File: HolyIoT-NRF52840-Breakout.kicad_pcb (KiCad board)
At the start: 2 copper layers, 45 x 35 mm, 7 parts, among them J1 Conn_01x13_Male, J2 Conn_01x09_Male, J3 Conn_01x11_Male, J4 Conn_01x13_Male, J5 Conn_01x09_Male, U1 HolyIOT_NRF52840

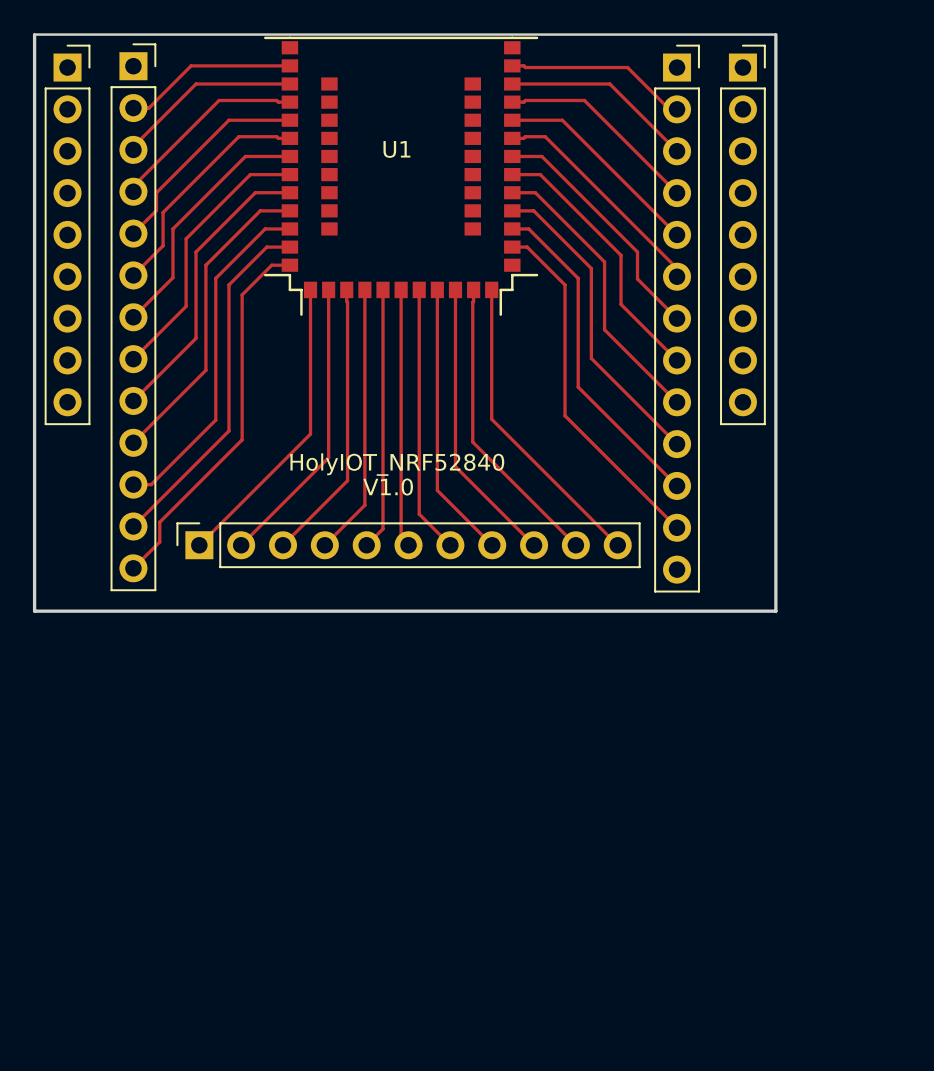
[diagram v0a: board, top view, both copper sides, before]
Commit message: Routing done
Last thing to do : labelling
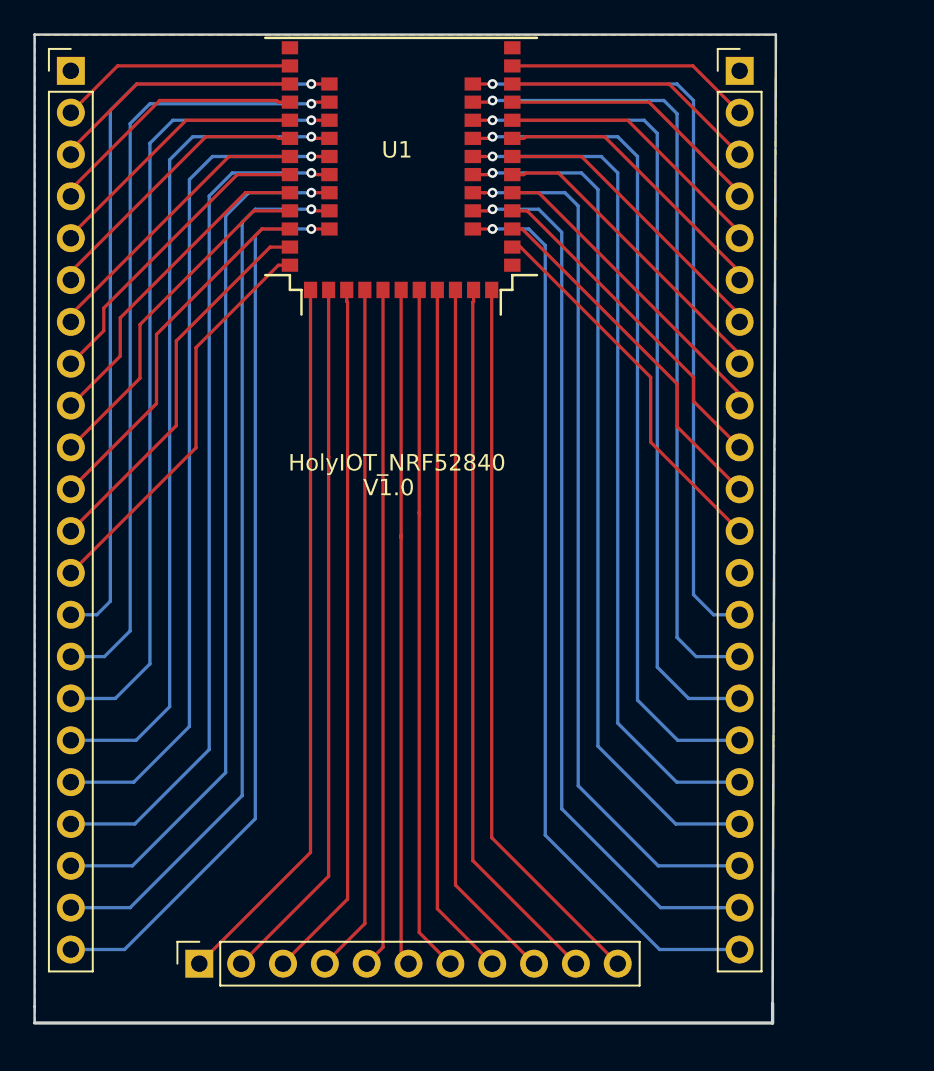
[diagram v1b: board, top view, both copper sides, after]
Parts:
- removed G***: LOGO, MWL:Serigraphie
- removed J4: Conn_01x13_Male, Connector_PinSocket_2.54mm:PinSocket_1x13_P2.54mm_Vertical
- removed J5: Conn_01x09_Male, Connector_PinSocket_2.54mm:PinSocket_1x09_P2.54mm_Vertical
- J1: value Conn_01x13_Male -> Conn_01x22_Male; footprint Connector_PinSocket_2.54mm:PinSocket_1x13_P2.54mm_Vertical -> Connector_PinHeader_2.54mm:PinHeader_1x22_P2.54mm_Vertical
- J2: value Conn_01x09_Male -> Conn_01x22_Male; footprint Connector_PinSocket_2.54mm:PinSocket_1x09_P2.54mm_Vertical -> Connector_PinHeader_2.54mm:PinHeader_1x22_P2.54mm_Vertical
- moved J2 40.8 mm to (138.8, 84.2)
- moved J3 25.4 mm to (106.0, 138.4)
- moved J1 3.81 mm to (98.2, 84.2)
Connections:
- J2 pad 1: Net-(J2-Pad1) -> GND
- U1 pad 14: Net-(J2-Pad1) -> Net-(J1-Pad14)
- U1 pad 15: Net-(J2-Pad2) -> Net-(J1-Pad15)
- U1 pad 16: Net-(J2-Pad3) -> Net-(J1-Pad16)
- U1 pad 17: Net-(J2-Pad4) -> Net-(J1-Pad17)
- U1 pad 18: Net-(J2-Pad5) -> Net-(J1-Pad18)
- U1 pad 19: Net-(J2-Pad6) -> Net-(J1-Pad19)
- U1 pad 20: Net-(J2-Pad7) -> Net-(J1-Pad20)
- U1 pad 21: Net-(J2-Pad8) -> Net-(J1-Pad21)
- U1 pad 22: Net-(J2-Pad9) -> Net-(J1-Pad22)
- U1 pad 23: Net-(J5-Pad1) -> Net-(J2-Pad14)
- U1 pad 24: Net-(J5-Pad2) -> Net-(J2-Pad15)
- U1 pad 25: Net-(J5-Pad3) -> Net-(J2-Pad16)
- U1 pad 26: Net-(J5-Pad4) -> Net-(J2-Pad17)
- U1 pad 27: Net-(J5-Pad5) -> Net-(J2-Pad18)
- U1 pad 28: Net-(J5-Pad6) -> Net-(J2-Pad19)
- U1 pad 29: Net-(J5-Pad7) -> Net-(J2-Pad20)
- U1 pad 30: Net-(J5-Pad8) -> Net-(J2-Pad21)
- U1 pad 31: Net-(J5-Pad9) -> Net-(J2-Pad22)
- U1 pad 33: Net-(J4-Pad2) -> Net-(J2-Pad2)
- U1 pad 34: Net-(J4-Pad3) -> Net-(J2-Pad3)
- U1 pad 35: Net-(J4-Pad4) -> Net-(J2-Pad4)
- U1 pad 36: Net-(J4-Pad5) -> Net-(J2-Pad5)
- U1 pad 37: Net-(J4-Pad6) -> Net-(J2-Pad6)
- U1 pad 38: Net-(J4-Pad7) -> Net-(J2-Pad7)
- U1 pad 39: Net-(J4-Pad8) -> Net-(J2-Pad8)
- U1 pad 40: Net-(J4-Pad9) -> Net-(J2-Pad9)
- U1 pad 41: Net-(J4-Pad10) -> Net-(J2-Pad10)
- U1 pad 42: Net-(J4-Pad11) -> Net-(J2-Pad11)
- U1 pad 43: Net-(J4-Pad12) -> Net-(J2-Pad12)
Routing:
- net Net-(J2-Pad22): track 0.00 -> 55.3 mm, vias 0 -> 1
- net Net-(J1-Pad22): track 0.00 -> 54.6 mm, vias 0 -> 1
- net Net-(J2-Pad21): track 0.00 -> 54.3 mm, vias 0 -> 1
- net Net-(J2-Pad20): track 0.00 -> 53.7 mm, vias 0 -> 1
- net Net-(J1-Pad21): track 0.00 -> 53.7 mm, vias 0 -> 1
- net Net-(J1-Pad20): track 0.00 -> 52.4 mm, vias 0 -> 1
- net Net-(J2-Pad19): track 0.00 -> 52.4 mm, vias 0 -> 1
- net Net-(J1-Pad19): track 0.00 -> 51.8 mm, vias 0 -> 1
- net Net-(J2-Pad18): track 0.00 -> 51.5 mm, vias 0 -> 1
- net Net-(J1-Pad18): track 0.00 -> 50.9 mm, vias 0 -> 1
- net Net-(J2-Pad17): track 0.00 -> 50.7 mm, vias 0 -> 1
- net Net-(J1-Pad17): track 0.00 -> 50.4 mm, vias 0 -> 1
- net Net-(J2-Pad16): track 0.00 -> 49.7 mm, vias 0 -> 1
- net Net-(J2-Pad15): track 0.00 -> 48.9 mm, vias 0 -> 1
- net Net-(J1-Pad16): track 0.00 -> 48.7 mm, vias 0 -> 1
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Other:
- board size 45 x 35 mm -> 45 x 60 mm
- net class Default: clearance 0.2 -> 0.3
- rule trace_clearance: 0.2 -> 0.3

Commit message: Add some serigraphie
Add some serigraphie
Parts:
- U1: value HolyIOT_NRF52840 -> HolyIOT_NRF52840_Module
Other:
- board text added: "GND"
- board text added: "P0.02"
- board text added: "P0.03"
- board text added: "P0.04"
- board text added: "P0.05"
- board text added: "P0.06"
- board text added: "P0.08"
- board text added: "P0.11"
- board text added: "P0.25"
- board text added: "P0.26"
- board text added: "P0.27"
- board text added: "P0.28"
- board text added: "P0.29"
- board text added: "P0.30"
- board text added: "P0.31"
- board text added: "P1.08"
- board text added: "P1.10"
- board text added: "P1.11"
- board text added: "P1.12"
- board text added: "P1.13"
- board text added: "P1.14"
- board text added: "P1.15"
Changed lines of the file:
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@@
   (general
     (thickness 1.6)
-    (drawings 9)
+    (drawings 31)
     (tracks 254)
     (zones 0)
@@
     (uvia_min_size 0.2)
     (uvia_min_drill 0.1)
-    (pcb_text_width 0.3)
-    (pcb_text_size 1.5 1.5)
+    (pcb_text_width 0.15)
+    (pcb_text_size 1 1)
     (mod_edge_width 0.15)
     (mod_text_size 1 1)
@@
       (effects (font (size 1 1) (thickness 0.15)))
     )
-    (fp_text value HolyIOT_NRF52840 (at 0 12) (layer F.SilkS)
+    (fp_text value HolyIOT_NRF52840_Module (at 0 12) (layer F.SilkS)
       (effects (font (size 1 1) (thickness 0.15)))
     )
@@
     )
   )
+  (gr_text P0.26 (at 102.2 137.4) (layer F.SilkS)
+    (effects (font (size 1 1) (thickness 0.15)))
+  )
+  (gr_text P0.06 (at 102.2 134.8) (layer F.SilkS)
+    (effects (font (size 1 1) (thickness 0.15)))
+  )
+  (gr_text P0.08 (at 102.2 132.4) (layer F.SilkS)
+    (effects (font (size 1 1) (thickness 0.15)))
+  )
+  (gr_text P0.27 (at 102.2 129.8) (layer F.SilkS)
+    (effects (font (size 1 1) (thickness 0.15)))
+  )
+  (gr_text P1.08 (at 102.2 127.2) (layer F.SilkS)
+    (effects (font (size 1 1) (thickness 0.15)))
+  )
+  (gr_text P0.11 (at 102.2 124.8) (layer F.SilkS)
+    (effects (font (size 1 1) (thickness 0.15)))
+  )
+  (gr_text P0.25 (at 102.2 122.2) (layer F.SilkS)
+    (effects (font (size 1 1) (thickness 0.15)))
+  )
+  (gr_text P1.12 (at 102.2 119.6) (layer F.SilkS)
+    (effects (font (size 1 1) (thickness 0.15)))
+  )
+  (gr_text P1.14 (at 102.2 117.2) (layer F.SilkS)
+    (effects (font (size 1 1) (thickness 0.15)))
+  )
+  (gr_text P0.05 (at 102.2 114.6) (layer F.SilkS)
+    (effects (font (size 1 1) (thickness 0.15)))
+  )
+  (gr_text "P0.04\n\n" (at 102.2 113) (layer F.SilkS)
+    (effects (font (size 1 1) (thickness 0.15)))
+  )
+  (gr_text "P0.31\n\n" (at 102.2 110.4) (layer F.SilkS)
+    (effects (font (size 1 1) (thickness 0.15)))
+  )
+  (gr_text "P0.30\n\n" (at 102.2 107.8) (layer F.SilkS)
+    (effects (font (size 1 1) (thickness 0.15)))
+  )
+  (gr_text "P0.29\n" (at 102.2 104.4) (layer F.SilkS)
+    (effects (font (size 1 1) (thickness 0.15)))
+  )
+  (gr_text "P0.28\n\n" (at 102.2 102.8) (layer F.SilkS)
+    (effects (font (size 1 1) (thickness 0.15)))
+  )
+  (gr_text "P0.02\n\n" (at 102.2 100.2) (layer F.SilkS)
+    (effects (font (size 1 1) (thickness 0.15)))
+  )
+  (gr_text "P0.03\n\n" (at 102.2 97.6) (layer F.SilkS)
+    (effects (font (size 1 1) (thickness 0.15)))
+  )
+  (gr_text "P1.15\n\n" (at 102.2 95.2) (layer F.SilkS)
+    (effects (font (size 1 1) (thickness 0.15)))
+  )
+  (gr_text "P1.13\n\n" (at 102.2 92.6) (layer F.SilkS)
+    (effects (font (size 1 1) (thickness 0.15)))
+  )
+  (gr_text "P1.11\n\n" (at 102.2 90) (layer F.SilkS)
+    (effects (font (size 1 1) (thickness 0.15)))
+  )
+  (gr_text "P1.10\n" (at 102.2 86.6) (layer F.SilkS)
+    (effects (font (size 1 1) (thickness 0.15)))
+  )
+  (gr_text GND (at 101.6 84) (layer F.SilkS)
+    (effects (font (size 1 1) (thickness 0.15)))
+  )
   (gr_line (start 96 141) (end 96 142) (layer Edge.Cuts) (width 0.15))

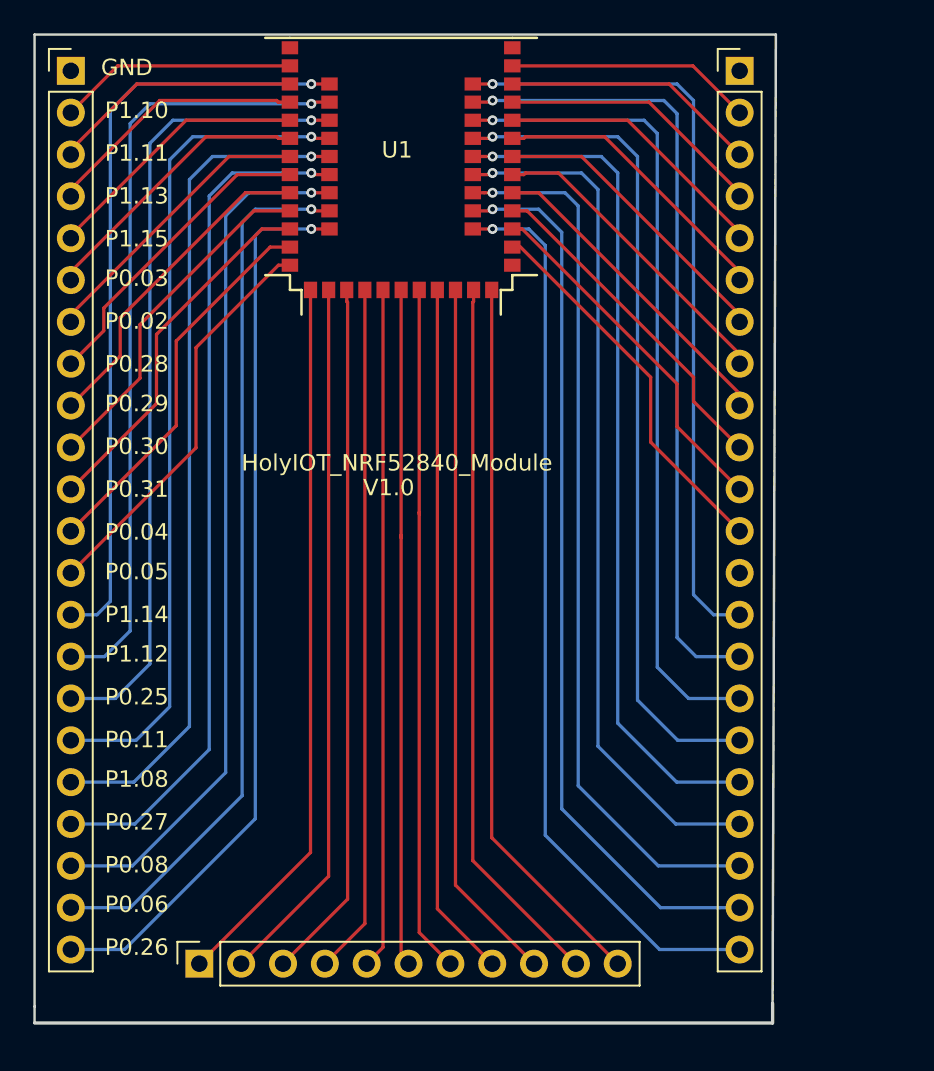
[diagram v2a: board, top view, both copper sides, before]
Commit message: Finish PCB V1.0
Add missing serigraphie
test via under pad
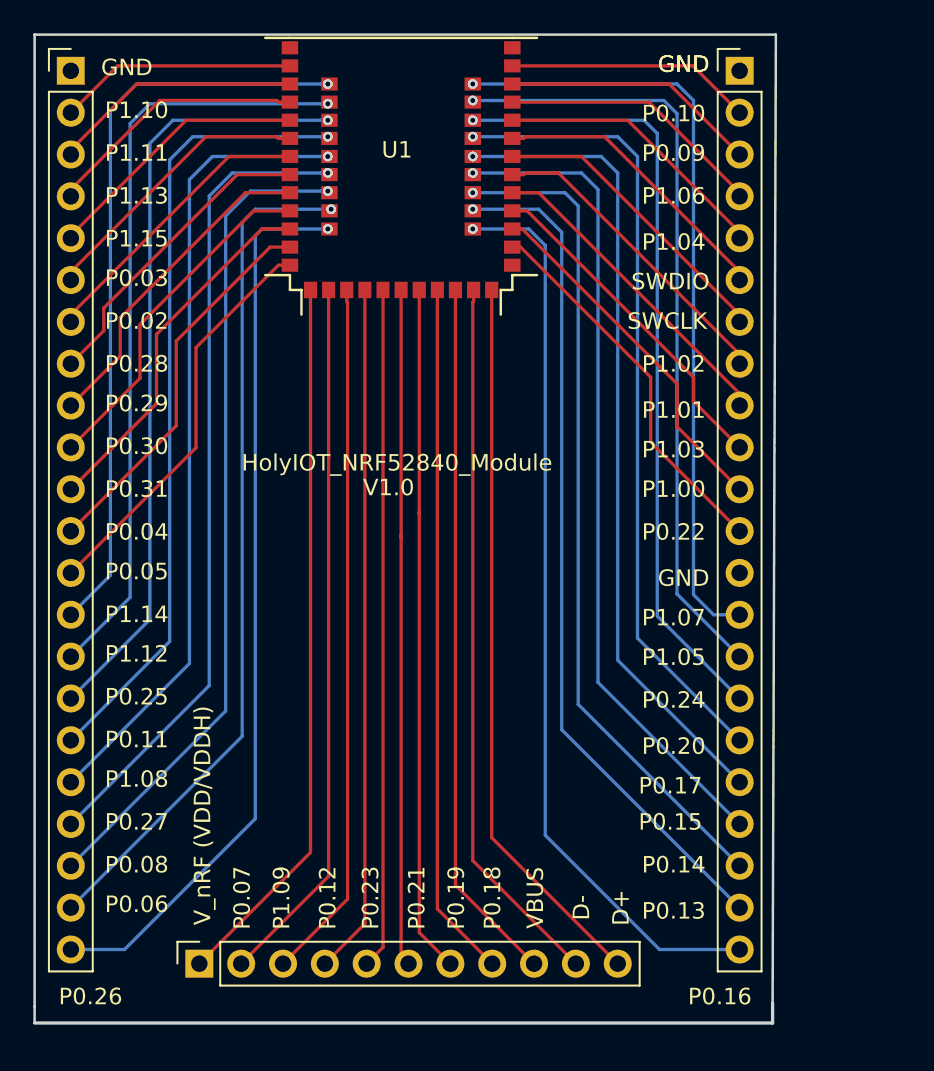
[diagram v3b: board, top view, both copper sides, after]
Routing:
- net Net-(J2-Pad20): track 53.7 -> 50.9 mm
- net Net-(J2-Pad21): track 54.3 -> 51.5 mm
- net Net-(J1-Pad17): track 50.4 -> 47.9 mm
- net Net-(J1-Pad19): track 51.8 -> 49.4 mm
- net Net-(J1-Pad18): track 50.9 -> 48.5 mm
- net Net-(J2-Pad19): track 52.4 -> 50.1 mm
- net Net-(J1-Pad20): track 52.4 -> 50.2 mm
- net Net-(J2-Pad17): track 50.7 -> 48.5 mm
- net Net-(J2-Pad18): track 51.5 -> 49.3 mm
- net Net-(J1-Pad21): track 53.7 -> 51.6 mm
- net Net-(J2-Pad16): track 49.7 -> 47.9 mm
- net Net-(J1-Pad16): track 48.7 -> 47.1 mm
- net Net-(J2-Pad15): track 48.9 -> 47.3 mm
- net Net-(J1-Pad15): track 47.7 -> 46.3 mm
- net Net-(J1-Pad14): track 46.5 -> 45.5 mm
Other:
- board text added: "D+"
- board text added: "D-"
- board text added: "P0.07"
- board text added: "P0.09"
- board text added: "P0.10"
- board text added: "P0.12"
- board text added: "P0.13"
- board text added: "P0.14"
- board text added: "P0.15"
- board text added: "P0.16"
- board text added: "P0.17"
- board text added: "P0.18"
- board text added: "P0.19"
- board text added: "P0.20"
- board text added: "P0.21"
- board text added: "P0.22"
- board text added: "P0.23"
- board text added: "P0.24"
- board text added: "P1.00"
- board text added: "P1.01"
- board text added: "P1.02"
- board text added: "P1.03"
- board text added: "P1.04"
- board text added: "P1.05"
- board text added: "P1.06"
- board text added: "P1.07"
- board text added: "P1.09"
- board text added: "SWCLK"
- board text added: "SWDIO"
- board text added: "VBUS"
- board text added: "V_nRF (VDD/VDDH)"

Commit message: Fornet the netlist
^^
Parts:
- U1: value HolyIOT_NRF52840_Module -> HolyIOT_NRF52840
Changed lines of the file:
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@@
       (effects (font (size 1 1) (thickness 0.15)))
     )
-    (fp_text value HolyIOT_NRF52840_Module (at 0 12) (layer F.SilkS)
+    (fp_text value HolyIOT_NRF52840 (at 0 12) (layer F.SilkS)
       (effects (font (size 1 1) (thickness 0.15)))
     )

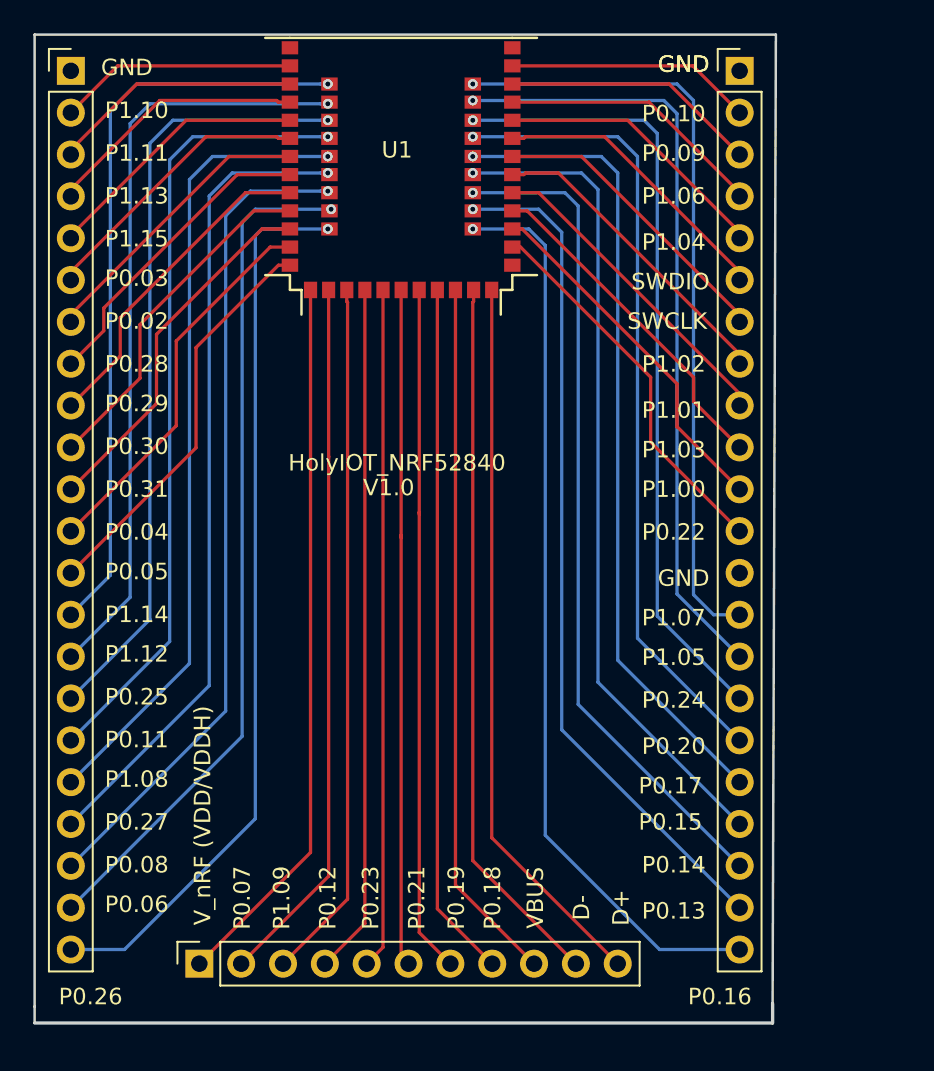
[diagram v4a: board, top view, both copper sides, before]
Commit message: micro-usb b
add micro-usb
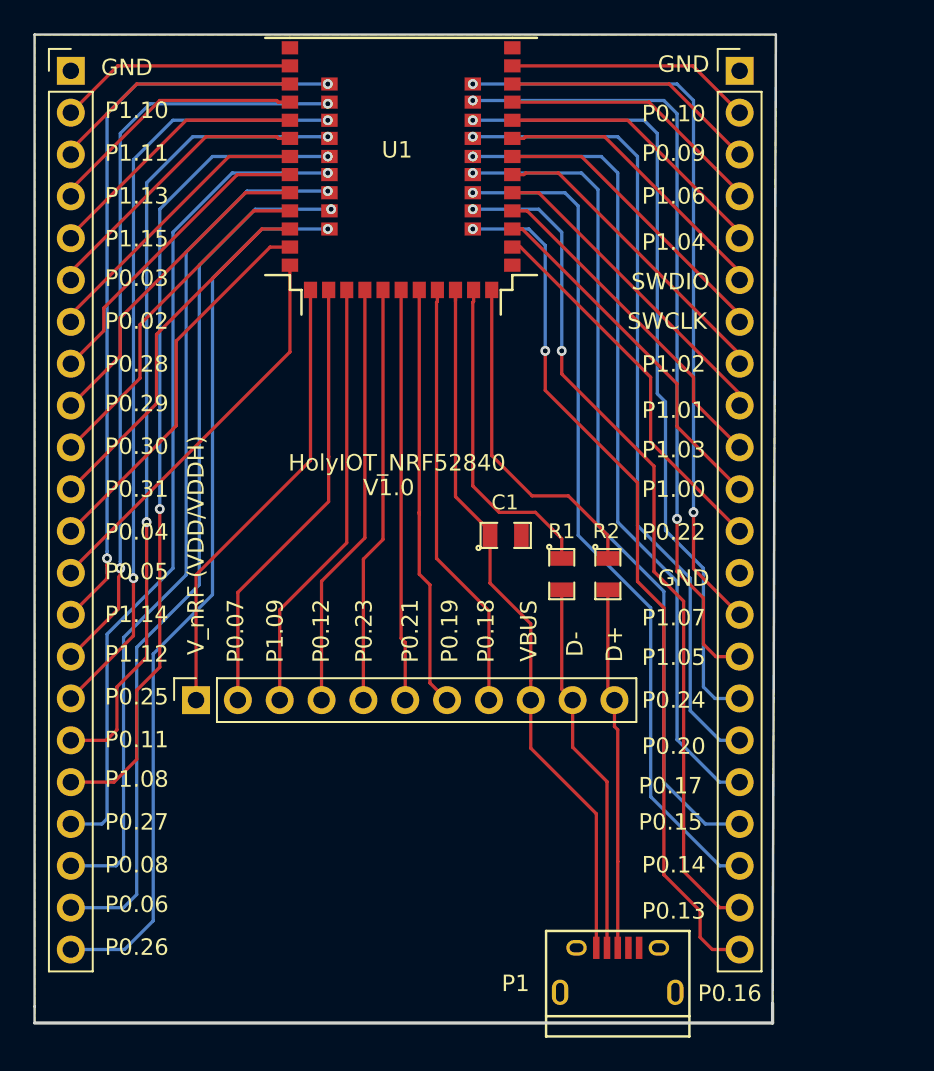
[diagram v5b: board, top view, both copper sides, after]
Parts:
- added C1: C, MWL:SM0805, F.Cu at (124.6, 112.4)
- added P1: USB_micro_B, MWL:USB_Micro-B, F.Cu at (131.4, 139.0)
- added R1: R, MWL:SM0805, F.Cu at (128.0, 114.8)
- added R2: R, MWL:SM0805, F.Cu at (130.8, 114.8)
- moved J3 16.0 mm to (105.8, 122.4)
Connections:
- U1 pad 45: Net-(J3-Pad11) -> Net-(R2-Pad1)
- U1 pad 46: Net-(J3-Pad10) -> Net-(R1-Pad1)
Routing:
- net Net-(J3-Pad11): track 44.1 -> 22.0 mm
- net Net-(J3-Pad10): track 43.5 -> 22.9 mm
- net Net-(R2-Pad1): track 0.00 -> 20.5 mm
- net Net-(R1-Pad1): track 0.00 -> 19.8 mm
- net Net-(J3-Pad6): track 41.3 -> 25.0 mm
- net Net-(J3-Pad7): track 41.8 -> 25.7 mm
- net Net-(J3-Pad8): track 42.3 -> 26.2 mm
- net Net-(J3-Pad3): track 42.5 -> 26.6 mm
- net Net-(J3-Pad4): track 41.9 -> 26.0 mm
- net Net-(J3-Pad5): track 41.3 -> 25.4 mm
- net Net-(J3-Pad2): track 43.2 -> 27.3 mm
- net Net-(J3-Pad1): track 43.7 -> 27.8 mm
- net Net-(J1-Pad21): track 51.6 -> 53.5 mm
- net Net-(J2-Pad22): track 55.3 -> 53.4 mm, vias 1 -> 2
- net Net-(J1-Pad20): track 50.2 -> 51.9 mm
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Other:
- board text added: "P0.18/RST"
